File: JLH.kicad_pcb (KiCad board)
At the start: 2 copper layers, 170 x 202 mm, 47 parts, among them J1 Вход, J2 Выход, J3 B2P-VH, Q1 КТ361Г, Q2 КТ801А, Q3 2Т803А, Q4 2Т803А, Q5 КТ361Г, Q6 КТ801А, Q7 2Т803А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

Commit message: Updated PCB
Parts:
- moved H2 0.50 mm to (27.5, 219.5)
- moved H4 0.50 mm to (146.5, 219.5)
- moved H6 0.50 mm to (182.5, 219.5)
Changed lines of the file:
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@@
   (general
     (thickness 1.6)
-    (drawings 16)
-    (tracks 202)
+    (drawings 19)
+    (tracks 200)
     (zones 0)
     (modules 47)
@@
   )
   (setup
-    (last_trace_width 1)
+    (last_trace_width 2.5)
     (user_trace_width 1)
     (user_trace_width 2.5)
@@
   )
   (module MountingHole:MountingHole_3.2mm_M3_Pad (layer F.Cu)
-    (at 27.5 220)
+    (at 27.5 219.5)
     (descr "Mounting Hole 3.2mm, M3")
     (tags "mounting hole 3.2mm m3")
@@
   )
   (module MountingHole:MountingHole_3.2mm_M3_Pad (layer F.Cu)
-    (at 146.5 220)
+    (at 146.5 219.5)
     (descr "Mounting Hole 3.2mm, M3")
     (tags "mounting hole 3.2mm m3")
@@
   )
   (module MountingHole:MountingHole_3.2mm_M3_Pad (layer F.Cu)
-    (at 182.5 220)
+    (at 182.5 219.5)
     (descr "Mounting Hole 3.2mm, M3")
     (tags "mounting hole 3.2mm m3")
@@
     (pad 1 thru_hole circle (at 0 0) (size 6.4 6.4) (drill 3.2) (layers *.Cu *.Mask))
   )
+  (dimension 7.5 (width 0.15) (layer Eco2.User)
+    (gr_text "7.500 mm" (at 35.8 223.25 270) (layer Eco2.User)
+      (effects (font (size 1 1) (thickness 0.15)))
+    )
+    (feature1 (pts (xy 27.5 227) (xy 35.086421 227)))
+    (feature2 (pts (xy 27.5 219.5) (xy 35.086421 219.5)))
+    (crossbar (pts (xy 34.5 219.5) (xy 34.5 227)))
+    (arrow1a (pts (xy 34.5 227) (xy 33.913579 225.873496)))
+    (arrow1b (pts (xy 34.5 227) (xy 35.086421 225.873496)))
+    (arrow2a (pts (xy 34.5 219.5) (xy 33.913579 220.626504)))
+    (arrow2b (pts (xy 34.5 219.5) (xy 35.086421 220.626504)))
+  )
+  (dimension 36 (width 0.12) (layer Eco2.User)
+    (gr_text "36.000 mm" (at 164.5 231.27) (layer Eco2.User)
+      (effects (font (size 1 1) (thickness 0.15)))
+    )
+    (feature1 (pts (xy 182.5 219.5) (xy 182.5 230.586421)))
+    (feature2 (pts (xy 146.5 219.5) (xy 146.5 230.586421)))
+    (crossbar (pts (xy 146.5 230) (xy 182.5 230)))
+    (arrow1a (pts (xy 182.5 230) (xy 181.373496 230.586421)))
+    (arrow1b (pts (xy 182.5 230) (xy 181.373496 229.413579)))
+    (arrow2a (pts (xy 146.5 230) (xy 147.626504 230.586421)))
+    (arrow2b (pts (xy 146.5 230) (xy 147.626504 229.413579)))
+  )
+  (dimension 7.5 (width 0.12) (layer Eco2.User)
+    (gr_text "7.500 mm" (at 23.75 231.27) (layer Eco2.User)
+      (effects (font (size 1 1) (thickness 0.15)))
+    )
+    (feature1 (pts (xy 20 219.5) (xy 20 230.586421)))
+    (feature2 (pts (xy 27.5 219.5) (xy 27.5 230.586421)))
+    (crossbar (pts (xy 27.5 230) (xy 20 230)))
+    (arrow1a (pts (xy 20 230) (xy 21.126504 229.413579)))
+    (arrow1b (pts (xy 20 230) (xy 21.126504 230.586421)))
+    (arrow2a (pts (xy 27.5 230) (xy 26.373496 229.413579)))
+    (arrow2b (pts (xy 27.5 230) (xy 26.373496 230.586421)))
+  )
   (gr_line (start 20 227) (end 20 25) (layer Edge.Cuts) (width 0.05))
   (gr_line (start 190 227) (end 20 227) (layer Edge.Cuts) (width 0.05))
@@
   (segment (start 117.5 70) (end 117.5 72.5) (width 2.5) (layer B.Cu) (net 5) (status 20))
   (segment (start 117.5 65.24) (end 117.5 70) (width 2.5) (layer B.Cu) (net 5) (status 10))
-  (segment (start 82.06 55.44) (end 82.94 55.44) (width 2.5) (layer B.Cu) (net 6))
-  (segment (start 72.5 65) (end 82.06 55.44) (width 2.5) (layer B.Cu) (net 6) (status 10))
-  (segment (start 82.94 55.44) (end 97.5 55.44) (width 2.5) (layer B.Cu) (net 6) (status 20))
-  (segment (start 107.5 55.44) (end 97.5 55.44) (width 2.5) (layer B.Cu) (net 6) (status 30))
+  (segment (start 107.5 55) (end 97.5 55) (width 2.5) (layer B.Cu) (net 6))
+  (segment (start 82.5 55) (end 97.5 55) (width 1) (layer B.Cu) (net 6))
+  (segment (start 72.5 65) (end 82.5 55) (width 1) (layer B.Cu) (net 6))
+  (segment (start 107.5 197) (end 97.5 197) (width 2.5) (layer B.Cu) (net 22))
+  (segment (start 72.5 187) (end 82.5 197) (width 1) (layer B.Cu) (net 22))
+  (segment (start 82.5 197) (end 97.5 197) (width 1) (layer B.Cu) (net 22))
   (segment (start 65 55) (end 65 50) (width 2.5) (layer B.Cu) (net 7) (status 10))
   (segment (start 67.26 50) (end 65 50) (width 2.5) (layer B.Cu) (net 7) (status 10))
@@
   (segment (start 91.48 174.5) (end 91.48 175.3) (width 2.5) (layer B.Cu) (net 20) (status 30))
   (segment (start 70.26 112.5) (end 65.54 112.5) (width 1) (layer B.Cu) (net 21) (status 30))
-  (segment (start 82.06 196.56) (end 82.94 196.56) (width 2.5) (layer B.Cu) (net 22))
-  (segment (start 107.5 196.56) (end 97.5 196.56) (width 2.5) (layer B.Cu) (net 22) (status 30))
-  (segment (start 82.94 196.56) (end 97.5 196.56) (width 2.5) (layer B.Cu) (net 22) (status 20))
-  (segment (start 72.5 187) (end 82.06 196.56) (width 2.5) (layer B.Cu) (net 22) (status 10))
   (segment (start 75.05 184.55) (end 76.88 184.55) (width 1) (layer B.Cu) (net 23))
   (segment (start 76.88 178.88) (end 75 177) (width 1) (layer B.Cu) (net 23) (status 20))

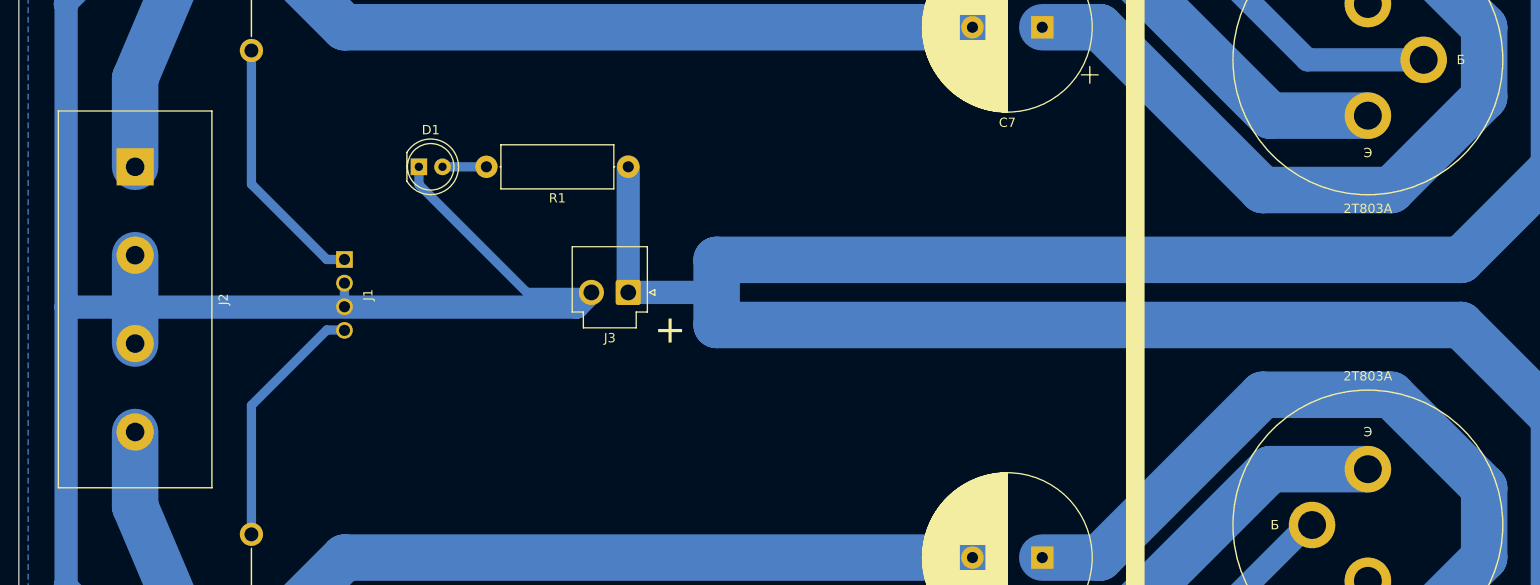
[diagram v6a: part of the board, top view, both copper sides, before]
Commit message: Added capacitors
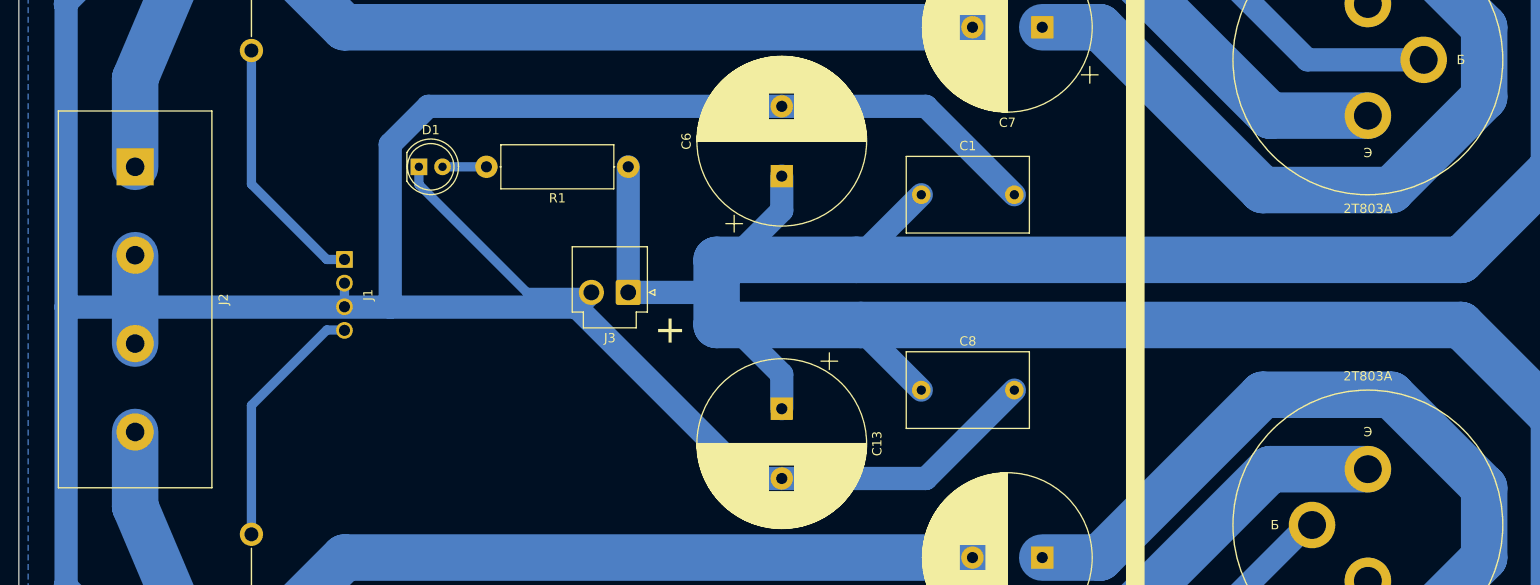
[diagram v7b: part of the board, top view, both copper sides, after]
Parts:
- added C1: 0,1 мкФ, Capacitor_THT:C_Rect_L13.0mm_W8.0mm_P10.00mm_FKS3_FKP3_MKS4, F.Cu at (117.0, 115.5)
- added C13: 2200 мкФ, Capacitor_THT:CP_Radial_D18.0mm_P7.50mm, F.Cu at (102.0, 138.5)
- added C6: 2200 мкФ, Capacitor_THT:CP_Radial_D18.0mm_P7.50mm, F.Cu at (102.0, 113.5)
- added C8: 0,1 мкФ, Capacitor_THT:C_Rect_L13.0mm_W8.0mm_P10.00mm_FKS3_FKP3_MKS4, F.Cu at (117.0, 136.5)
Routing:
- net GND: track 623.6 -> 772.4 mm
- net /Левый канал/VCC: track 564.9 -> 610.3 mm

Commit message: Updated PCB
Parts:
- moved H1 1.00 mm to (27.5, 33.5)
- moved H2 1.00 mm to (27.5, 218.5)
- moved H3 1.00 mm to (146.5, 33.5)
- moved H4 1.00 mm to (146.5, 218.5)
- moved H5 1.00 mm to (182.5, 33.5)
- moved H6 1.00 mm to (182.5, 218.5)
- moved J1 0.27 mm to (55.0, 122.2)
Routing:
- net GND: track 772.4 -> 666.0 mm
- net Net-(C4-Pad2): track 199.6 -> 154.6 mm
- net Net-(C11-Pad2): track 199.6 -> 154.6 mm
- net /Левый канал/VCC: track 610.3 -> 593.0 mm
- net Net-(Q6-Pad3): track 90.4 -> 88.9 mm
- net Net-(Q2-Pad3): track 102.9 -> 101.4 mm
- added copper zone on F.Cu, net GND
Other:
- board size 170 x 202 mm -> 170 x 200 mm
